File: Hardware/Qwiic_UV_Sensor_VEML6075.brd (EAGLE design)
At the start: 38.1 x 38.1 mm, 28 parts, among them J1 GATORGATOR_MINI, J2 GATORGATOR_MINI, J3 GATORGATOR_MINI, J4 GATORGATOR_MINI, J5 GATORGATOR_MINI, J6 GATORGATOR_MINI, J7 GATORGATOR_MINI, J8 GATORGATOR_MINI, U1 VEML6075

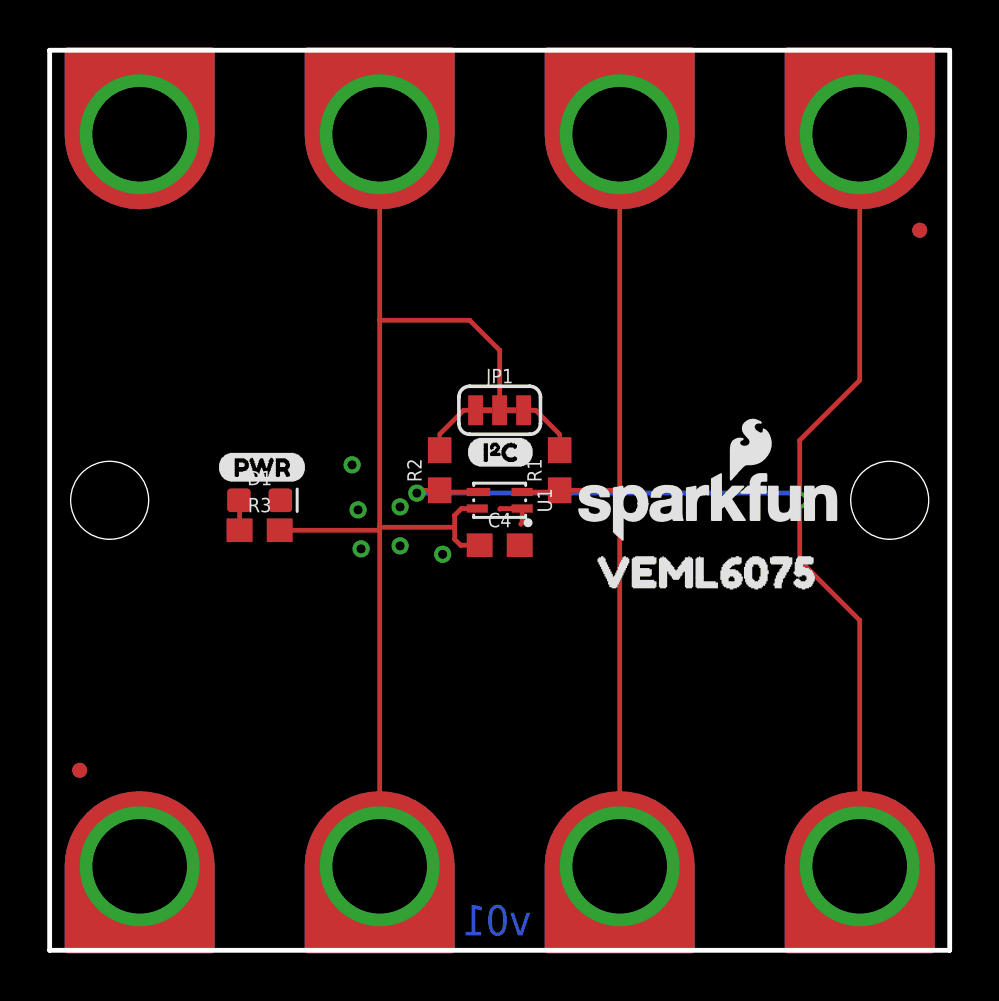
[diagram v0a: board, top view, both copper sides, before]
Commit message: resizing and adding silk
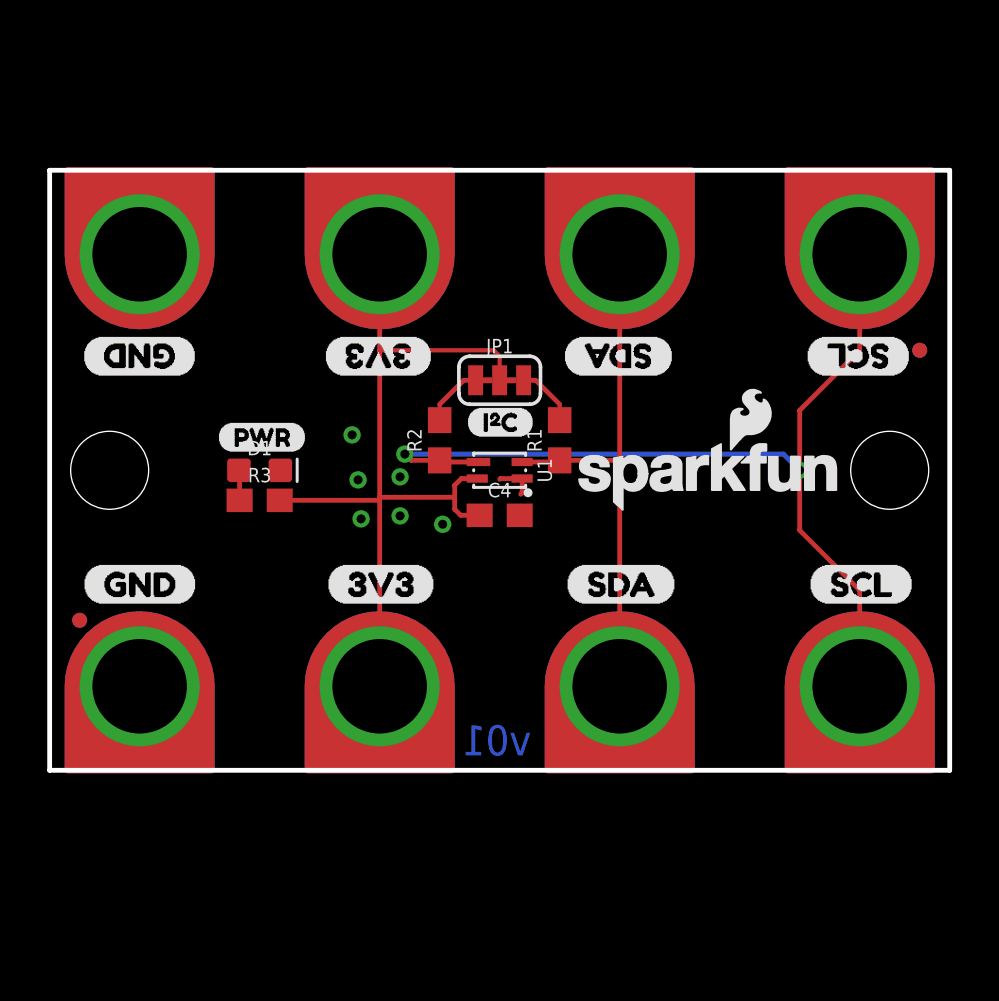
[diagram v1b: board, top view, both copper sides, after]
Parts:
- removed U$6: (no value), Qwiic_UV_Sensor_VEML6075:_VEML60750
- added U$11, U$17, U$21, U$5: (no value), buzzard_labels:SCL2
- added U$12, U$15, U$20, U$7: (no value), buzzard_labels:SDA1
- added U$13, U$18, U$4, U$9: (no value), buzzard_labels:GND0
- added U$14, U$19, U$3, U$8: (no value), buzzard_labels:3V33
- moved J1 7.62 mm to (34.3, 11.4)
- moved J2 7.62 mm to (24.1, 11.4)
- moved J3 7.62 mm to (14.0, 11.4)
- moved J4 7.62 mm to (3.81, 11.4)
- moved JP2 6.35 mm to (1.27, 14.0)
- moved JP5 6.35 mm to (1.27, 14.0)
- moved JP6 5.08 mm to (36.8, 25.4)
- moved JP7 5.08 mm to (36.8, 25.4)
- moved J5 5.08 mm to (3.81, 29.2)
- moved J6 5.08 mm to (14.0, 29.2)
- moved J7 5.08 mm to (24.1, 29.2)
- moved J8 5.08 mm to (34.3, 29.2)
- moved C4 1.27 mm to (19.1, 18.4)
- moved D1 1.27 mm to (8.89, 20.3)
- moved JP1 1.27 mm to (19.1, 24.1)
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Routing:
- net 3.3V: track 49.8 -> 35.1 mm
- net SDA: track 35.2 -> 22.5 mm
- net SCL: track 52.1 -> 40.6 mm
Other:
- board size 38.1 x 38.1 mm -> 38.1 x 25.4 mm
- board text removed: "Jim Lindblom"

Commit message: adding labelling, removing pullup jumper
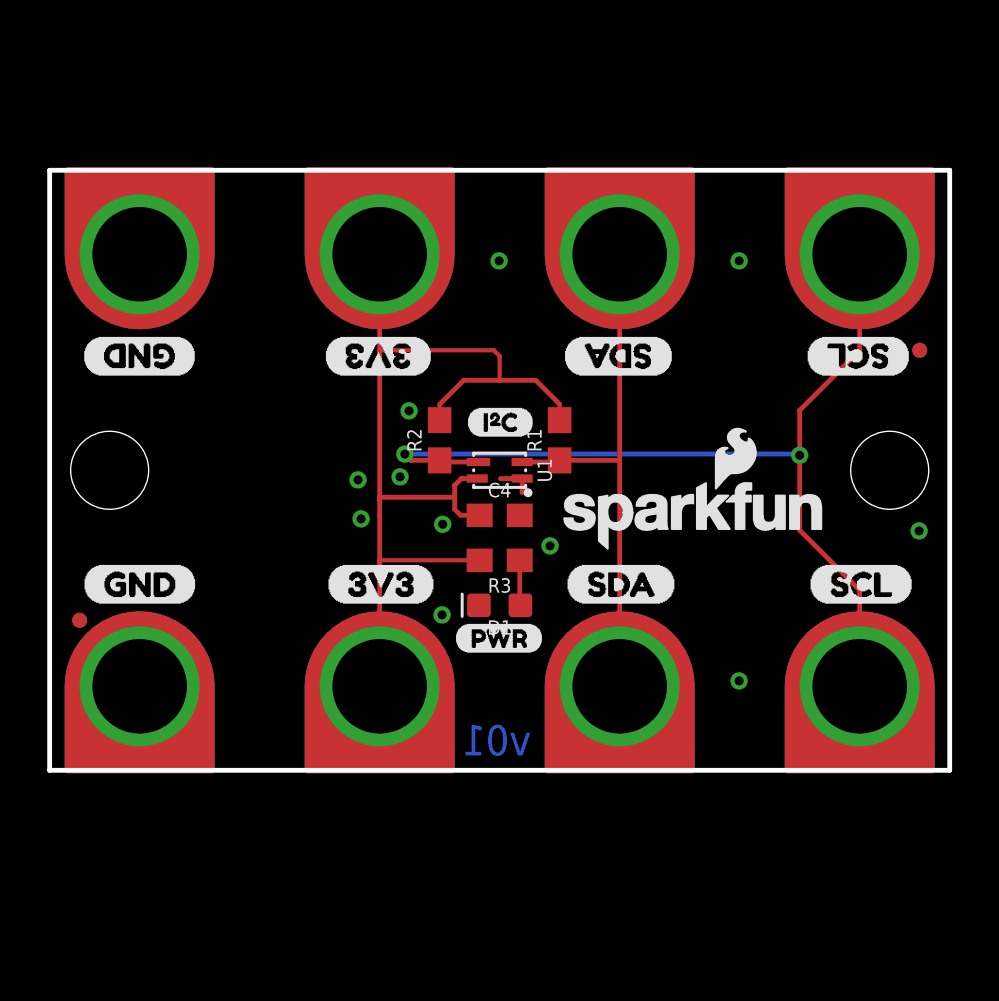
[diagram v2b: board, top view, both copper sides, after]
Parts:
- removed JP1: I2C, SparkFun-Jumpers:SMT-JUMPER_3_2-NC_TRACE_SILK
- R1, R2: value 2.2k -> 10k
- moved LOGO1 15.3 mm to (19.1, 8.89)
- moved U$16 13.2 mm to (17.1, 13.2)
- moved D1 11.7 mm to (19.1, 14.6), turned to 180 degrees
- moved R3 10.5 mm to (19.1, 16.5), turned to 180 degrees
- moved U$1 1.77 mm to (27.3, 18.4)
- moved U$2 1.77 mm to (27.3, 18.4)
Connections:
- removed net N$4: JP1.3, R1.2
- removed net N$5: JP1.1, R2.2
- net 3.3V: now also R1.2, R2.2; no longer JP1.2
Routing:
- net 3.3V: track 35.1 -> 42.4 mm
- net N$4: track 2.62 -> 0.00 mm
- net N$5: track 2.62 -> 0.00 mm
- net N$3: track 1.28 -> 1.92 mm
- net GND: track 1.65 -> 1.52 mm, vias 6 -> 11

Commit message: adding protection circuitry
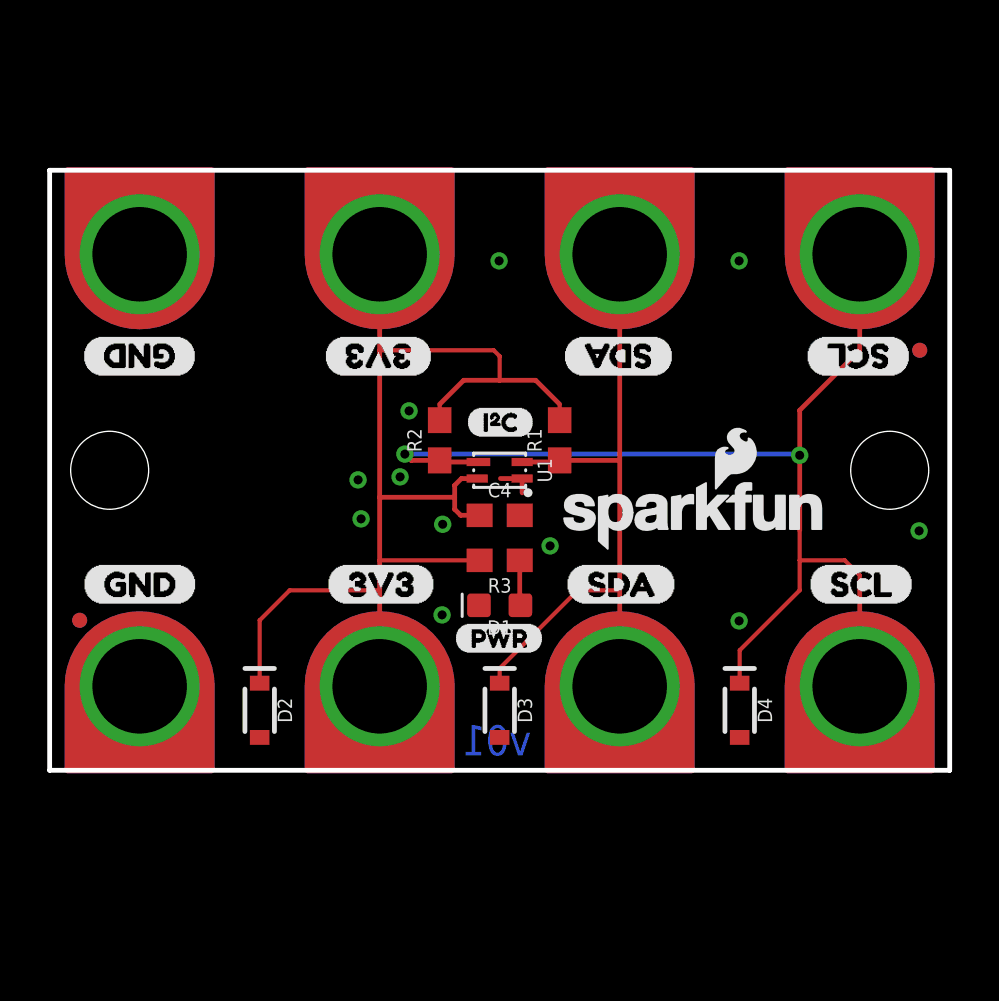
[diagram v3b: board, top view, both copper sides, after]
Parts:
- added D2, D3, D4: 3.6V, SparkFun-DiscreteSemi:SOD-323
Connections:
- net 3.3V: now also D2.C
- net GND: now also D2.A, D3.A, D4.A
- net SCL: now also D4.C
- net SDA: now also D3.C
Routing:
- net 3.3V: track 42.4 -> 50.7 mm
- net SCL: track 40.4 -> 47.7 mm
- net SDA: track 22.5 -> 29.5 mm
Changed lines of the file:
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@@
 <?xml version="1.0" encoding="utf-8"?>
 <!DOCTYPE eagle SYSTEM "eagle.dtd">
-<eagle version="9.1.0">
+<eagle version="9.3.1">
 <drawing>
 <settings>
@@
 <element name="U$20" library="buzzard_labels" package="SDA1" value="" x="26.416" y="15.494" smashed="yes" rot="MR0"/>
 <element name="U$21" library="buzzard_labels" package="SCL2" value="" x="36.449" y="15.494" smashed="yes" rot="MR0"/>
+<element name="D2" library="SparkFun-DiscreteSemi" package="SOD-323" value="3.6V" x="8.89" y="10.16" smashed="yes" rot="R270">
+<attribute name="NAME" x="9.652" y="10.16" size="0.6096" layer="25" font="vector" ratio="20" rot="R270" align="bottom-center"/>
+<attribute name="PROD_ID" value="DIO-08199" x="8.89" y="10.16" size="1.778" layer="27" rot="R270" display="off"/>
+<attribute name="VALUE" x="8.128" y="10.16" size="0.6096" layer="27" font="vector" ratio="20" rot="R270" align="top-center"/>
+</element>
+<element name="D3" library="SparkFun-DiscreteSemi" package="SOD-323" value="3.6V" x="19.05" y="10.16" smashed="yes" rot="R270">
+<attribute name="NAME" x="19.812" y="10.16" size="0.6096" layer="25" font="vector" ratio="20" rot="R270" align="bottom-center"/>
+<attribute name="PROD_ID" value="DIO-08199" x="19.05" y="10.16" size="1.778" layer="27" rot="R270" display="off"/>
+<attribute name="VALUE" x="18.288" y="10.16" size="0.6096" layer="27" font="vector" ratio="20" rot="R270" align="top-center"/>
+</element>
+<element name="D4" library="SparkFun-DiscreteSemi" package="SOD-323" value="3.6V" x="29.21" y="10.16" smashed="yes" rot="R270">
+<attribute name="NAME" x="29.972" y="10.16" size="0.6096" layer="25" font="vector" ratio="20" rot="R270" align="bottom-center"/>
+<attribute name="PROD_ID" value="DIO-08199" x="29.21" y="10.16" size="1.778" layer="27" rot="R270" display="off"/>
+<attribute name="VALUE" x="28.448" y="10.16" size="0.6096" layer="27" font="vector" ratio="20" rot="R270" align="top-center"/>
+</element>
 </elements>
 <signals>
@@
 <wire x1="13.97" y1="29.464" x2="13.97" y2="25.4" width="0.2032" layer="1"/>
 <wire x1="13.97" y1="25.4" x2="13.97" y2="19.177" width="0.2032" layer="1"/>
-<wire x1="13.97" y1="19.177" x2="13.97" y2="19.05" width="0.2032" layer="1"/>
-<wire x1="13.97" y1="19.05" x2="13.97" y2="18.415" width="0.2032" layer="1"/>
 <wire x1="17.145" y1="19.177" x2="13.97" y2="19.177" width="0.2032" layer="1"/>
 <wire x1="13.97" y1="25.4" x2="18.796" y2="25.4" width="0.1778" layer="1"/>
@@
 <wire x1="16.51" y1="22.44" x2="16.51" y2="23.114" width="0.1778" layer="1"/>
 <wire x1="16.51" y1="23.114" x2="17.526" y2="24.13" width="0.2032" layer="1"/>
-<wire x1="20.574" y1="24.13" x2="20.574" y2="24.13" width="0.2032" layer="1"/>
 <wire x1="17.526" y1="24.13" x2="19.05" y2="24.13" width="0.2032" layer="1"/>
 <wire x1="19.05" y1="24.13" x2="20.574" y2="24.13" width="0.2032" layer="1"/>
 <wire x1="18.796" y1="25.4" x2="19.05" y2="25.146" width="0.1778" layer="1"/>
 <wire x1="19.05" y1="25.146" x2="19.05" y2="24.13" width="0.1778" layer="1"/>
-<wire x1="13.97" y1="18.415" x2="13.97" y2="16.51" width="0.2032" layer="1"/>
-<wire x1="13.97" y1="16.51" x2="13.97" y2="11.176" width="0.2032" layer="1"/>
+<wire x1="13.97" y1="19.177" x2="13.97" y2="16.51" width="0.2032" layer="1"/>
+<wire x1="13.97" y1="16.51" x2="13.97" y2="15.24" width="0.2032" layer="1"/>
+<wire x1="13.97" y1="15.24" x2="13.97" y2="11.176" width="0.2032" layer="1"/>
 <wire x1="18.2" y1="16.51" x2="13.97" y2="16.51" width="0.1778" layer="1"/>
 <wire x1="17.399003125" y1="18.415" x2="18.2" y2="18.415" width="0.2032" layer="1"/>
+<contactref element="D2" pad="C"/>
+<wire x1="8.89" y1="11.31" x2="8.89" y2="13.97" width="0.1778" layer="1"/>
+<wire x1="8.89" y1="13.97" x2="10.16" y2="15.24" width="0.1778" layer="1"/>
+<wire x1="10.16" y1="15.24" x2="13.97" y2="15.24" width="0.1778" layer="1"/>
 </signal>
 <signal name="GND">
@@
 <via x="19.0246" y="29.1846" extent="1-16" drill="0.381"/>
 <via x="29.1846" y="29.1846" extent="1-16" drill="0.381"/>
-<via x="29.1846" y="11.4046" extent="1-16" drill="0.381"/>
+<via x="29.1846" y="13.9446" extent="1-16" drill="0.381"/>
 <via x="36.8046" y="17.7546" extent="1-16" drill="0.381"/>
 <via x="15.2146" y="22.8346" extent="1-16" drill="0.381"/>
+<contactref element="D2" pad="A"/>
+<contactref element="D3" pad="A"/>
+<contactref element="D4" pad="A"/>
 </signal>
 <signal name="N$3">
@@
 <wire x1="21.52" y1="20.67" x2="21.59" y2="20.74" width="0.2032" layer="1"/>
 <wire x1="24.13" y1="29.464" x2="24.13" y2="20.701" width="0.2032" layer="1"/>
-<wire x1="24.13" y1="20.701" x2="24.13" y2="11.176" width="0.2032" layer="1"/>
+<wire x1="24.13" y1="20.701" x2="24.13" y2="15.24" width="0.2032" layer="1"/>
+<wire x1="24.13" y1="15.24" x2="24.13" y2="11.176" width="0.2032" layer="1"/>
 <wire x1="21.59" y1="20.74" x2="24.091" y2="20.74" width="0.2032" layer="1"/>
 <wire x1="24.091" y1="20.74" x2="24.13" y2="20.701" width="0.2032" layer="1"/>
+<contactref element="D3" pad="C"/>
+<wire x1="19.05" y1="11.31" x2="19.05" y2="11.938" width="0.1778" layer="1"/>
+<wire x1="22.352" y1="15.24" x2="24.13" y2="15.24" width="0.1778" layer="1"/>
+<wire x1="19.05" y1="11.938" x2="22.352" y2="15.24" width="0.1778" layer="1"/>
 </signal>
 <signal name="SCL">
@@
 <wire x1="34.29" y1="25.4" x2="31.75" y2="22.86" width="0.2032" layer="1"/>
 <wire x1="31.75" y1="22.86" x2="31.75" y2="20.955" width="0.2032" layer="1"/>
-<wire x1="31.75" y1="20.955" x2="31.75" y2="17.78" width="0.2032" layer="1"/>
-<wire x1="31.75" y1="17.78" x2="34.29" y2="15.24" width="0.2032" layer="1"/>
-<wire x1="34.29" y1="15.24" x2="34.29" y2="11.176" width="0.2032" layer="1"/>
+<wire x1="31.75" y1="17.78" x2="31.75" y2="20.955" width="0.2032" layer="1"/>
+<wire x1="34.29" y1="11.176" x2="34.29" y2="15.24" width="0.2032" layer="1"/>
 <wire x1="16.51" y1="20.74" x2="15.3003625" y2="20.74" width="0.2032" layer="1"/>
 <wire x1="15.3003625" y1="20.74" x2="15.03568125" y2="21.00468125" width="0.2032" layer="1"/>
@@
 <wire x1="31.70031875" y1="21.00468125" x2="31.75" y2="20.955" width="0.2032" layer="16"/>
 <via x="31.75" y="20.955" extent="1-16" drill="0.381"/>
+<contactref element="D4" pad="C"/>
+<wire x1="29.21" y1="11.31" x2="29.21" y2="12.7" width="0.1778" layer="1"/>
+<wire x1="29.21" y1="12.7" x2="31.75" y2="15.24" width="0.1778" layer="1"/>
+<wire x1="31.75" y1="15.24" x2="31.75" y2="16.51" width="0.1778" layer="1"/>
+<wire x1="31.75" y1="16.51" x2="31.75" y2="17.78" width="0.1778" layer="1"/>
+<wire x1="34.29" y1="15.24" x2="34.29" y2="15.875" width="0.1778" layer="1"/>
+<wire x1="34.29" y1="15.875" x2="33.655" y2="16.51" width="0.1778" layer="1"/>
+<wire x1="33.655" y1="16.51" x2="31.75" y2="16.51" width="0.1778" layer="1"/>
 </signal>
 </signals>

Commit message: finalizing silk and schematic before design review
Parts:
- removed U$10: (no value), Labels:I_SUPER2_C-()-03
- added U$22, U$23: (no value), GatorBit_Final_for_Silk#01#png (3):GATORBIT_FINAL_FOR_SILK#01#PNG
- added U$6: (no value), buzzard_labels (4):GATOR#UV5
- moved U$1 2.17 mm to (28.1, 20.4)
- moved U$2 2.13 mm to (27.9, 20.4)
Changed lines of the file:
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@@
 <?xml version="1.0" encoding="utf-8"?>
 <!DOCTYPE eagle SYSTEM "eagle.dtd">
-<eagle version="9.3.1">
+<eagle version="9.1.0">
 <drawing>
 <settings>
@@
 <attribute name="VALUE" value="10k" x="17.272" y="21.59" size="0.6096" layer="27" font="vector" ratio="20" rot="R90" align="top-center"/>
 </element>
-<element name="U$2" library="SparkFun-Aesthetics" package="SFE_LOGO_NAME_FLAME_.1" value="SFE_LOGO_NAME_FLAME.1_INCH" x="27.305" y="18.415" smashed="yes" rot="MR0"/>
+<element name="U$2" library="SparkFun-Aesthetics" package="SFE_LOGO_NAME_FLAME_.1" value="SFE_LOGO_NAME_FLAME.1_INCH" x="27.94" y="20.447" smashed="yes" rot="MR0"/>
 <element name="LOGO1" library="SparkFun-Aesthetics" package="OSHW-LOGO-MINI" value="OSHW-LOGOMINI" x="19.05" y="8.89" smashed="yes" rot="MR0"/>
-<element name="U$1" library="SparkFun-Aesthetics" package="SFE_LOGO_NAME_FLAME_.1" value="SFE_LOGO_NAME_FLAME.1_INCH" x="27.305" y="18.415" smashed="yes"/>
+<element name="U$1" library="SparkFun-Aesthetics" package="SFE_LOGO_NAME_FLAME_.1" value="SFE_LOGO_NAME_FLAME.1_INCH" x="28.067" y="20.447" smashed="yes"/>
 <element name="JP3" library="SparkFun" package="STAND-OFF" value="STAND-OFF" x="2.54" y="20.32" smashed="yes"/>
 <element name="JP4" library="SparkFun" package="STAND-OFF" value="STAND-OFF" x="35.56" y="20.32" smashed="yes" rot="R90"/>
@@
 <element name="JP5" library="SparkFun" package="MICRO-FIDUCIAL" value="FIDUCIALUFIDUCIAL" x="1.27" y="13.97" smashed="yes"/>
 <element name="JP7" library="SparkFun" package="MICRO-FIDUCIAL" value="FIDUCIALUFIDUCIAL" x="36.83" y="25.4" smashed="yes" rot="MR0"/>
-<element name="U$10" library="Labels" package="I_SUPER2_C-()-03" value="" x="17.653" y="22.352" smashed="yes"/>
 <element name="U$16" library="Labels" package="PWR-()-03" value="" x="17.145" y="13.208" smashed="yes"/>
 <element name="J1" library="SparkFun-Connectors" package="GATOR_MINI" value="GATORGATOR_MINI" x="34.29" y="11.43" smashed="yes"/>
@@
 <attribute name="VALUE" x="28.448" y="10.16" size="0.6096" layer="27" font="vector" ratio="20" rot="R270" align="top-center"/>
 </element>
+<element name="U$6" library="buzzard_labels (4)" package="GATOR#UV5" value="" x="24.13" y="19.05"/>
+<element name="U$22" library="GatorBit_Final_for_Silk#01#png (3)" package="GATORBIT_FINAL_FOR_SILK#01#PNG" value="" x="8.763" y="20.828"/>
+<element name="U$23" library="GatorBit_Final_for_Silk#01#png (3)" package="GATORBIT_FINAL_FOR_SILK#01#PNG" value="" x="8.763" y="20.828" rot="MR0"/>
 </elements>
 <signals>

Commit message: post checklist changes
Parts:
- added Q1: 2.5A/30V/105mΩ, SparkFun-DiscreteSemi:SOT23-3
- added R4: 10k, SparkFun-Resistors:0603
- added U$10: (no value), SparkFun-Aesthetics:ORDERING_INSTRUCTIONS
- moved JP2 7.65 mm to (0.64, 6.35)
- moved JP5 7.65 mm to (0.64, 6.35)
- moved J5 7.62 mm to (3.81, 21.6)
- moved J6 7.62 mm to (14.0, 21.6)
- moved J7 7.62 mm to (24.1, 21.6)
- moved J8 7.62 mm to (34.3, 21.6)
- moved JP3 7.62 mm to (2.54, 12.7)
- moved JP4 7.62 mm to (35.6, 12.7)
- moved LOGO1 7.62 mm to (19.1, 1.27)
- moved R3 7.62 mm to (19.1, 8.89)
- moved U$11 7.62 mm to (32.1, 17.5)
- moved U$12 7.62 mm to (21.8, 17.5)
- moved U$13 7.62 mm to (6.22, 17.5)
- moved U$14 7.62 mm to (16.3, 17.5)
- moved U$15 7.62 mm to (26.4, 17.5)
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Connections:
- new net N$1: J3.P$2, J6.P$2, Q1.3
- new net N$4: D2.A, Q1.1, R4.2
- net 3.3V: now also Q1.2; no longer J3.P$2, J6.P$2
- net GND: now also R4.1; no longer D2.A
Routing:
- net N$1: track 0.00 -> 23.4 mm, vias 0 -> 1
- net 3.3V: track 50.7 -> 39.6 mm
- net N$4: track 0.00 -> 6.33 mm
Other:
- board text added: "Black Gloss Soldermask"
- board text added: "Units in Inches"

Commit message: updating to VEML6070
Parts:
- added R5: 10k, SparkFun-Resistors:0603
- added R6: 300k, SparkFun-Resistors:0603
- U1: value VEML6075 -> VEML6070"; device SparkFun-Sensors:VEML6075_A3OP -> SparkFun-Sensors:VEML6070
- moved R1 1.42 mm to (22.2, 15.2)
- moved U1 1.27 mm to (19.1, 14.0)
- moved R2 1.27 mm to (16.5, 15.2)
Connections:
- new net ACK: R5.1, U1.2
- new net N$2: R6.2, U1.4
- net 3.3V: now also R5.2, U1.6; no longer U1.4
- net GND: now also R6.1
- net SCL: now also U1.5; no longer U1.3
- net SDA: now also U1.3; no longer U1.2
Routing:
- net ACK: track 0.00 -> 4.57 mm
- net 3.3V: track 39.6 -> 42.4 mm
- net SDA: track 29.5 -> 32.2 mm
- net N$2: track 0.00 -> 1.41 mm
- net GND: track 1.52 -> 2.00 mm, vias 11 -> 12

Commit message: post review changes
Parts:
- added U$24: (no value), buzzard_labels (4):GATOR#UV5
- moved LOGO1 2.54 mm to (19.1, 3.81)
- moved U$1 1.91 mm to (28.2, 10.9)
- moved U$2 1.91 mm to (28.1, 10.9)
- moved U$6 1.78 mm to (24.1, 9.65)
- moved U1 1.27 mm to (19.1, 12.7)
- moved R1 1.27 mm to (22.2, 14.0)
- moved R2 1.27 mm to (16.5, 14.0)
- moved R5 1.27 mm to (24.1, 14.0)
- moved R6 1.27 mm to (19.1, 14.6)
- moved JP6 0.63 mm to (36.8, 18.4)
- moved JP7 0.63 mm to (36.8, 18.4)
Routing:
- net 3.3V: track 42.4 -> 38.4 mm
- net GND: vias 12 -> 13
